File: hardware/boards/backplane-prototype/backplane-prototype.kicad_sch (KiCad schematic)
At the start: 17 parts, among them J1 DC_IN, J10 SLOT_3_IO, J11 SLOT_4_IO, J12 SLOT_5_IO, J13 SLOT_6_IO, J2 SLOT_1, J3 SLOT_2, J4 SLOT_3, J5 SLOT_4, J6 SLOT_5, J7 SLOT_6, J8 SLOT_1_IO, J9 SLOT_2_IO

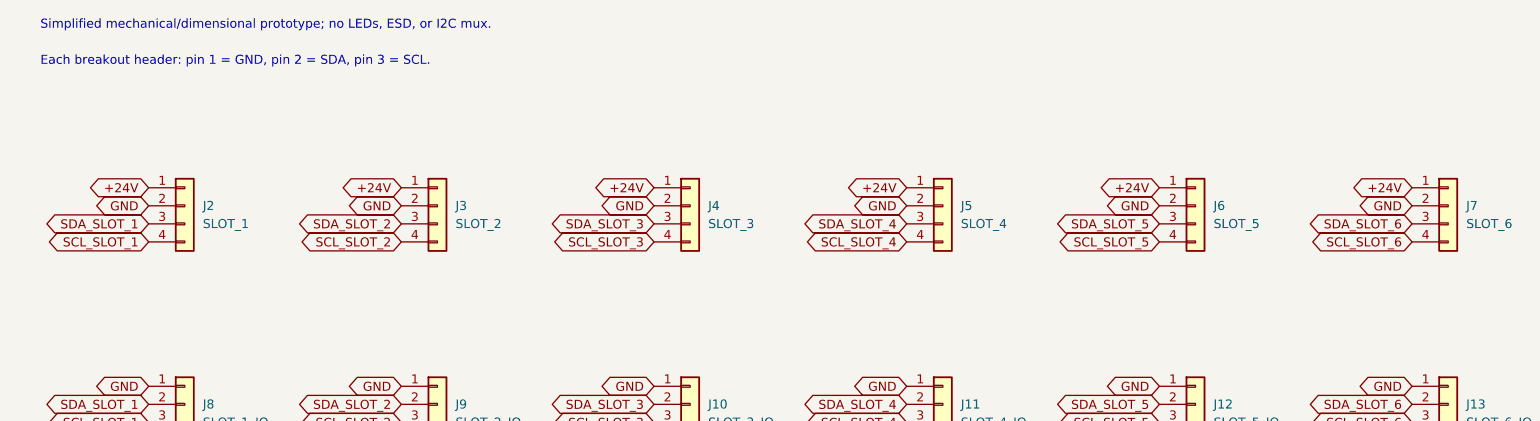
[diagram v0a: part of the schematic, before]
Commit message: Mirror prototype slot pinout changes
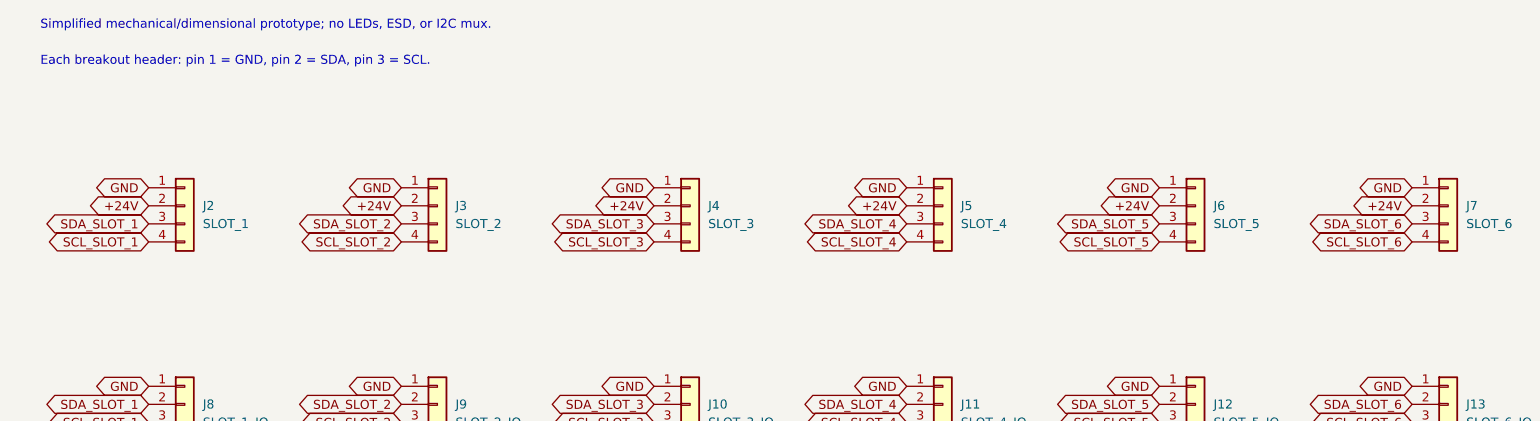
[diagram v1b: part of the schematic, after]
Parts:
- J2, J3, J4, J5, J6, J7: Pinout 1=+24V; 2=GND; 3=SDA; 4=SCL -> 1=GND; 2=+24V; 3=SDA; 4=SCL
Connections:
- net +24V: now also J2.2 (Pin_2), J3.2 (Pin_2), J4.2 (Pin_2), J5.2 (Pin_2), J6.2 (Pin_2), J7.2 (Pin_2); no longer J2.1 (Pin_1), J3.1 (Pin_1), J4.1 (Pin_1), J5.1 (Pin_1), J6.1 (Pin_1), J7.1 (Pin_1)
- net GND: now also J2.1 (Pin_1), J3.1 (Pin_1), J4.1 (Pin_1), J5.1 (Pin_1), J6.1 (Pin_1), J7.1 (Pin_1); no longer J2.2 (Pin_2), J3.2 (Pin_2), J4.2 (Pin_2), J5.2 (Pin_2), J6.2 (Pin_2), J7.2 (Pin_2)

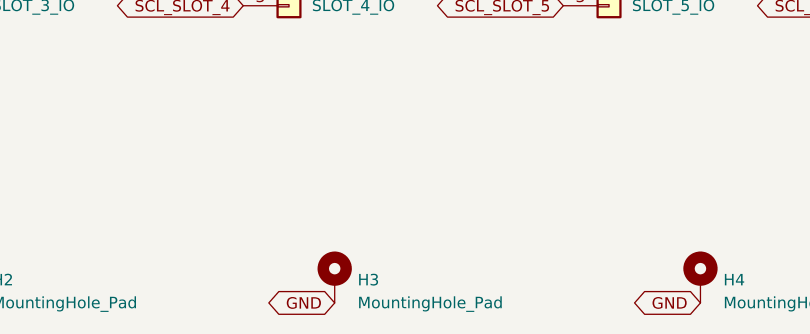
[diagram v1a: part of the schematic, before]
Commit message: Compact prototype backplane layout
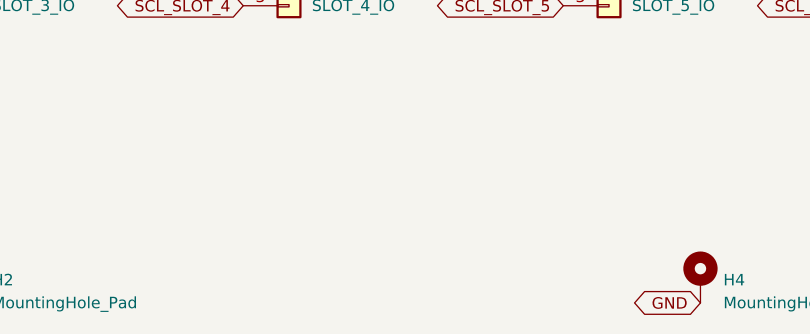
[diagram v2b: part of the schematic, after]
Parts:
- removed H3: MountingHole_Pad, MountingHole:MountingHole_3.2mm_M3_Pad_Via, symbol Mechanical:MountingHole_Pad
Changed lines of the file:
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@@
-	(global_label "GND"
-		(shape bidirectional)
-		(at 157.48 109.22 180)
-		(effects
-			(font
-				(size 1.27 1.27)
-			)
-			(justify right)
-		)
-		(property "Intersheetrefs" "${INTERSHEET_REFS}"
-			(at 157.48 109.22 0)
-			(hide yes)
-			(show_name no)
-			(do_not_autoplace no)
-			(effects
-				(font
-					(size 1.27 1.27)
-				)
-			)
-		)
-	)
 	(global_label "GND"
 		(shape bidirectional)
@@
 					(unit 1)
 				)
-			)
-		)
-	)
-	(symbol
-		(lib_id "Mechanical:MountingHole_Pad")
-		(at 157.48 106.68 0)
-		(unit 1)
-		(body_style 1)
-		(exclude_from_sim no)
-		(in_bom no)
-		(on_board yes)
-		(in_pos_files yes)
-		(dnp no)
-		(fields_autoplaced yes)
-		(property "Reference" "H3"
-			(at 160.02 106.68 0)
-			(show_name no)
-			(do_not_autoplace no)
-			(effects
-				(font
-					(size 1.27 1.27)
-				)
-				(justify left)
-			)
-		)
-		(property "Value" "MountingHole_Pad"
-			(at 160.02 109.22 0)
-			(show_name no)
-			(do_not_autoplace no)
-			(effects
-				(font
-					(size 1.27 1.27)
-				)
-				(justify left)
-			)
-		)
-		(property "Footprint" "MountingHole:MountingHole_3.2mm_M3_Pad_Via"
-			(at 157.48 106.68 0)
-			(hide yes)
-			(show_name no)
-			(do_not_autoplace no)
-			(effects
-				(font
-					(size 1.27 1.27)
-				)
-			)
-		)
-		(property "Datasheet" ""
-			(at 157.48 106.68 0)
-			(hide yes)
-			(show_name no)
-			(do_not_autoplace no)
-			(effects
-				(font
-					(size 1.27 1.27)
-				)
-			)
-		)
-		(property "Description" "Grounded M3 mounting hole"
-			(at 157.48 106.68 0)
-			(hide yes)
-			(show_name no)
-			(do_not_autoplace no)
-			(effects
-				(font
-					(size 1.27 1.27)
-				)
-			)
-		)
-		(pin "1"
-		)
-		(instances
-			(project "backplane-prototype"
-				(path "/348cc909-6345-4013-9bef-98714057a65b"
-					(reference "H3")
-					(unit 1)
-				)

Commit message: Checkpoint current hardware revisions
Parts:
- removed J10: SLOT_3_IO, Connector_PinHeader_2.54mm:PinHeader_1x03_P2.54mm_Vertical, symbol Connector_Generic:Conn_01x03
- removed J11: SLOT_4_IO, Connector_PinHeader_2.54mm:PinHeader_1x03_P2.54mm_Vertical, symbol Connector_Generic:Conn_01x03
- removed J12: SLOT_5_IO, Connector_PinHeader_2.54mm:PinHeader_1x03_P2.54mm_Vertical, symbol Connector_Generic:Conn_01x03
- removed J13: SLOT_6_IO, Connector_PinHeader_2.54mm:PinHeader_1x03_P2.54mm_Vertical, symbol Connector_Generic:Conn_01x03
- removed J8: SLOT_1_IO, Connector_PinHeader_2.54mm:PinHeader_1x03_P2.54mm_Vertical, symbol Connector_Generic:Conn_01x03
- removed J9: SLOT_2_IO, Connector_PinHeader_2.54mm:PinHeader_1x03_P2.54mm_Vertical, symbol Connector_Generic:Conn_01x03
- added H3, H5, H6: MountingHole_Pad, MountingHole:MountingHole_2.2mm_M2_Pad_Via, symbol Mechanical:MountingHole_Pad
- added J8: i2c_busses, Connector_PinHeader_1.00mm:PinHeader_2x07_P1.00mm_Vertical, symbol Connector_Generic:Conn_02x07_Odd_Even
- H1, H2, H4: footprint MountingHole:MountingHole_3.2mm_M3_Pad_Via -> MountingHole:MountingHole_2.2mm_M2_Pad_Via
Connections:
- net GND: now also H3.1, H5.1, H6.1, J8.1 (Pin_1)
- net SCL_SLOT_1: now also J8.14 (Pin_14)
- net SCL_SLOT_2: now also J8.12 (Pin_12)
- net SCL_SLOT_3: now also J8.10 (Pin_10)
- net SCL_SLOT_4: now also J8.8 (Pin_8)
- net SCL_SLOT_5: now also J8.6 (Pin_6)
- net SCL_SLOT_6: now also J8.4 (Pin_4)
- net SDA_SLOT_1: now also J8.13 (Pin_13)
- net SDA_SLOT_2: now also J8.11 (Pin_11)
- net SDA_SLOT_3: now also J8.9 (Pin_9)
- net SDA_SLOT_4: now also J8.7 (Pin_7)
- net SDA_SLOT_5: now also J8.5 (Pin_5)
- net SDA_SLOT_6: now also J8.3 (Pin_3)
- new net +3V3: J8.2 (Pin_2)
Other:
- moved on the sheet: H1, H2, H4, J1

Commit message: chore: checkpoint workspace changes
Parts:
- added D3: PESD5V0S2BT,215, Package_TO_SOT_SMD:SOT-23, symbol backplane-backpack:PESD_Dual_SOT23
- added R3, R4: 4.7k 1%, Resistor_SMD:R_0603_1608Metric, symbol Device:R
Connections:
- net +3V3: now also R3.1, R4.1
- net GND: now also D3.3 (GND)
- new net: D3.2 (IO2), R4.2
- new net: D3.1 (IO1), R3.2
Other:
- note added: "TODO: confirm pullups are / are-not already on the carrier module. If they are, DNP!"

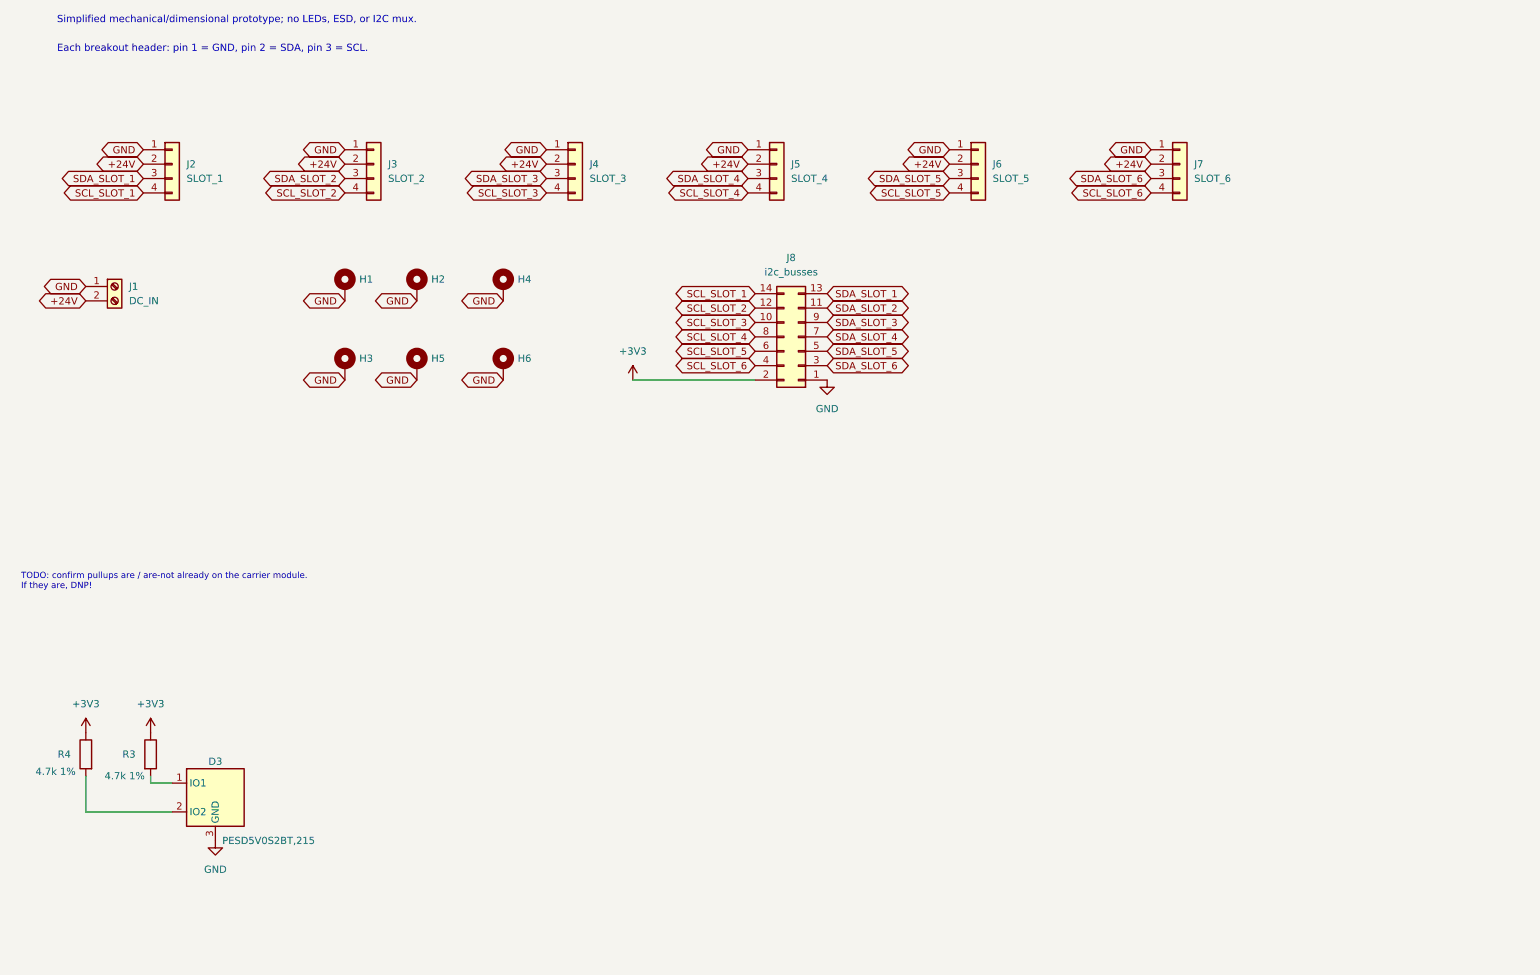
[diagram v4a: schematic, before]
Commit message: feat: add per-slot I2C ESD protection
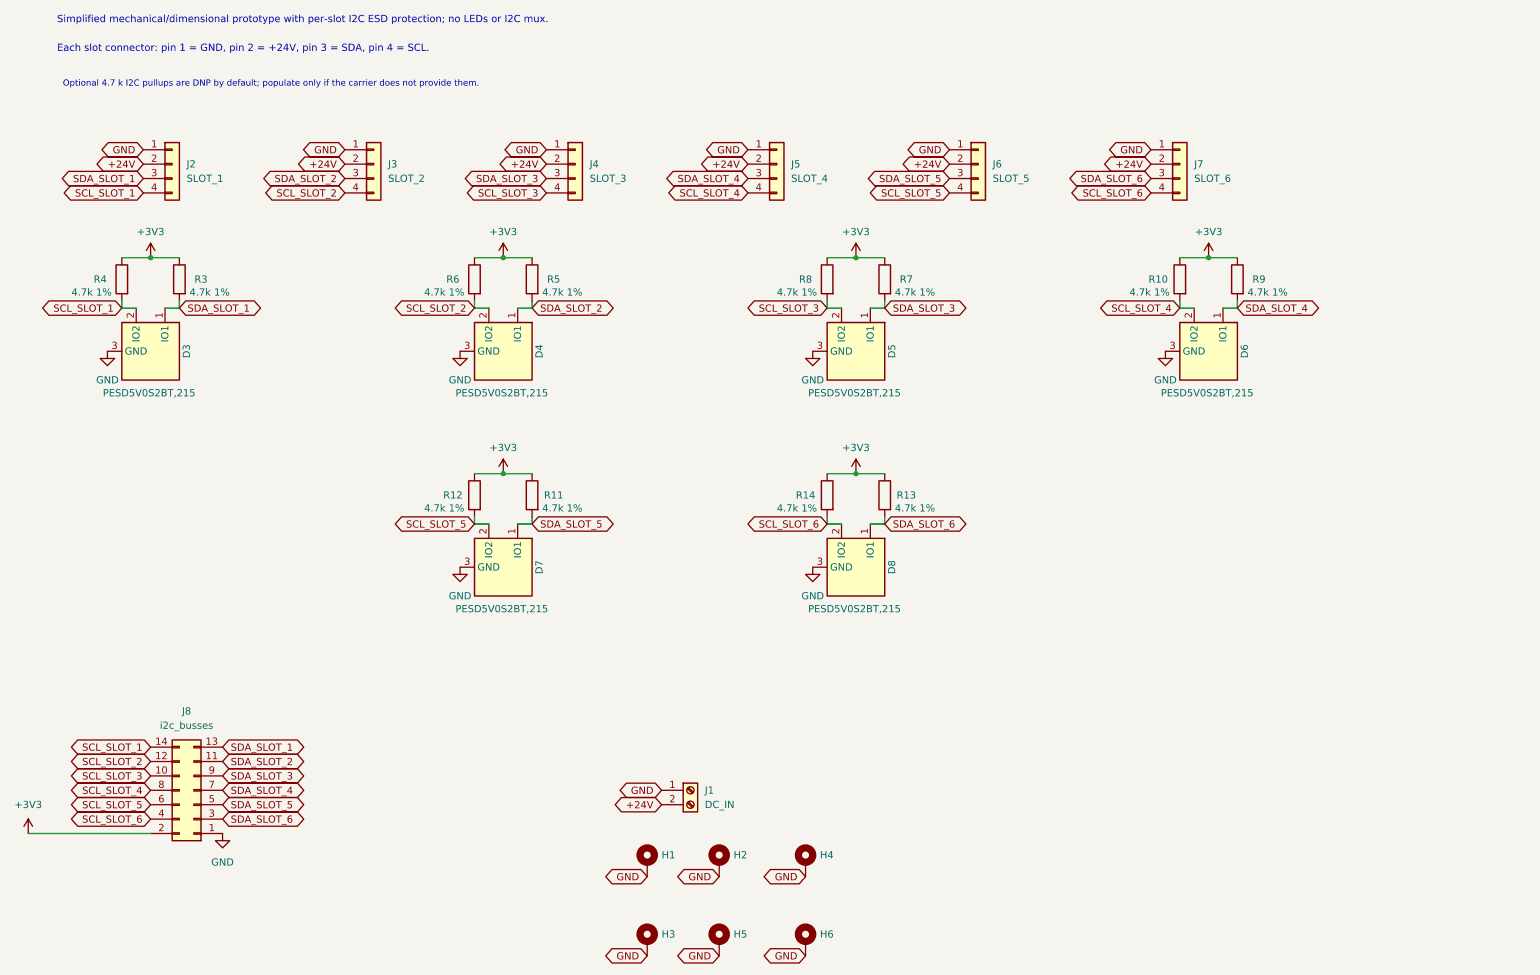
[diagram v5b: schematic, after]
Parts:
- added D4, D5, D6, D7, D8: PESD5V0S2BT,215, Package_TO_SOT_SMD:SOT-23, symbol backplane-backpack:PESD_Dual_SOT23
- added R10, R11, R12, R13, R14, R5, R6, R7, R8, R9: 4.7k 1%, Resistor_SMD:R_0603_1608Metric, symbol Device:R
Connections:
- net +3V3: now also R10.1, R11.1, R12.1, R13.1, R14.1, R5.1, R6.1, R7.1, R8.1, R9.1
- net GND: now also D4.3 (GND), D5.3 (GND), D6.3 (GND), D7.3 (GND), D8.3 (GND)
- net SCL_SLOT_1: now also D3.2 (IO2), R4.2
- net SCL_SLOT_2: now also D4.2 (IO2), R6.2
- net SCL_SLOT_3: now also D5.2 (IO2), R8.2
- net SCL_SLOT_4: now also D6.2 (IO2), R10.2
- net SCL_SLOT_5: now also D7.2 (IO2), R12.2
- net SCL_SLOT_6: now also D8.2 (IO2), R14.2
- net SDA_SLOT_1: now also D3.1 (IO1), R3.2
- net SDA_SLOT_2: now also D4.1 (IO1), R5.2
- net SDA_SLOT_3: now also D5.1 (IO1), R7.2
- net SDA_SLOT_4: now also D6.1 (IO1), R9.2
- net SDA_SLOT_5: now also D7.1 (IO1), R11.2
- net SDA_SLOT_6: now also D8.1 (IO1), R13.2
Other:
- note added: "Each slot connector: pin 1 = GND, pin 2 = +24V, pin 3 = SDA, pin 4 = SCL."
- note added: "Optional 4.7 k I2C pullups are DNP by default; populate only if the carrier does not provide them."
- note added: "Simplified mechanical/dimensional prototype with per-slot I2C ESD protection; no LEDs or I2C mux."
- note removed: "Each breakout header: pin 1 = GND, pin 2 = SDA, pin 3 = SCL."
- note removed: "Simplified mechanical/dimensional prototype; no LEDs, ESD, or I2C mux."
- note removed: "TODO: confirm pullups are / are-not already on the carrier module. If they are, DNP!"
- moved on the sheet: H1, H2, H3, H4, H5, H6, J1, J8, R3, R4

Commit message: fix: mark prototype power rails as driven
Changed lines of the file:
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@@
 	(wire
 		(pts
-			(xy 20.32 163.83) (xy 41.91 163.83)
-		)
-		(stroke
-			(width 0)
-			(type default)
-		)
-	)
-	(wire
-		(pts
 			(xy 41.91 62.23) (xy 46.99 62.23)
 		)
@@
 		)
 	)
+	(wire
+		(pts
+			(xy 54.61 163.83) (xy 60.96 163.83)
+		)
+		(stroke
+			(width 0)
+			(type default)
+		)
+	)
+	(junction
+		(at 54.61 163.83)
+		(diameter 0)
+		(color 0 0 0 0)
+	)
+	(symbol
+		(lib_id "power:PWR_FLAG")
+		(at 31.75 170.18 0)
+		(unit 1)
+		(body_style 1)
+		(exclude_from_sim no)
+		(in_bom yes)
+		(on_board yes)
+		(in_pos_files yes)
+		(dnp no)
+		(property "Reference" "#FLG0101"
+			(at 31.75 176.53 0)
+			(show_name no)
+			(do_not_autoplace no)
+			(effects
+				(font
+					(size 1.27 1.27)
+				)
+				(hide yes)
+			)
+		)
+		(property "Value" "PWR_FLAG"
+			(at 31.75 173.98999999999998 0)
+			(show_name no)
+			(do_not_autoplace no)
+			(effects
+				(font
+					(size 1.27 1.27)
+				)
+			)
+		)
+		(property "Footprint" ""
+			(at 31.75 170.18 0)
+			(hide yes)
+			(show_name no)
+			(do_not_autoplace no)
+			(effects
+				(font
+					(size 1.27 1.27)
+				)
+			)
+		)
+		(property "Datasheet" ""
+			(at 31.75 170.18 0)
+			(hide yes)
+			(show_name no)
+			(do_not_autoplace no)
+			(effects
+				(font
+					(size 1.27 1.27)
+				)
+			)
+		)
+		(property "Description" "Special symbol for telling ERC where power comes from"
+			(at 31.75 170.18 0)
+			(hide yes)
+			(show_name no)
+			(do_not_autoplace no)
+			(effects
+				(font
+					(size 1.27 1.27)
+				)
+			)
+		)
+		(pin "1"
+		)
+		(instances
+			(project "backplane-prototype"
+				(path "/348cc909-6345-4013-9bef-98714057a65b"
+					(reference "#FLG0101")
+					(unit 1)
+				)
+			)
+		)
+	)
+	(symbol
+		(lib_id "power:PWR_FLAG")
+		(at 60.96 170.18 0)
+		(unit 1)
+		(body_style 1)
+		(exclude_from_sim no)
+		(in_bom yes)
+		(on_board yes)
+		(in_pos_files yes)
+		(dnp no)
+		(property "Reference" "#FLG0102"
+			(at 60.96 176.53 0)
+			(show_name no)
+			(do_not_autoplace no)
+			(effects
+				(font
+					(size 1.27 1.27)
+				)
+				(hide yes)
+			)
+		)
+		(property "Value" "PWR_FLAG"
+			(at 60.96 173.98999999999998 0)
+			(show_name no)
+			(do_not_autoplace no)
+			(effects
+				(font
+					(size 1.27 1.27)
+				)
+			)
+		)
+		(property "Footprint" ""
+			(at 60.96 170.18 0)
+			(hide yes)
+			(show_name no)
+			(do_not_autoplace no)
+			(effects
+				(font
+					(size 1.27 1.27)
+				)
+			)
+		)
+		(property "Datasheet" ""
+			(at 60.96 170.18 0)
+			(hide yes)
+			(show_name no)
+			(do_not_autoplace no)
+			(effects
+				(font
+					(size 1.27 1.27)
+				)
+			)
+		)
+		(property "Description" "Special symbol for telling ERC where power comes from"
+			(at 60.96 170.18 0)
+			(hide yes)
+			(show_name no)
+			(do_not_autoplace no)
+			(effects
+				(font
+					(size 1.27 1.27)
+				)
+			)
+		)
+		(pin "1"
+		)
+		(instances
+			(project "backplane-prototype"
+				(path "/348cc909-6345-4013-9bef-98714057a65b"
+					(reference "#FLG0102")
+					(unit 1)
+				)
+			)
+		)
+	)
+	(wire
+		(pts
+			(xy 20.32 163.83) (xy 31.75 163.83)
+		)
+		(stroke
+			(width 0)
+			(type default)
+		)
+	)
+	(wire
+		(pts
+			(xy 31.75 163.83) (xy 41.91 163.83)
+		)
+		(stroke
+			(width 0)
+			(type default)
+		)
+	)
+	(wire
+		(pts
+			(xy 31.75 163.83) (xy 31.75 170.18)
+		)
+		(stroke
+			(width 0)
+			(type default)
+		)
+	)
+	(junction
+		(at 31.75 163.83)
+		(diameter 0)
+		(color 0 0 0 0)
+	)
+	(wire
+		(pts
+			(xy 60.96 163.83) (xy 60.96 170.18)
+		)
+		(stroke
+			(width 0)
+			(type default)
+		)
+	)

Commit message: feat: add shift-register slot power control
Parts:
- J2: Pinout 1=GND; 2=+24V; 3=SDA; 4=SCL -> 1=GND; 2=SLOT_1_PWR_SW; 3=SDA; 4=SCL
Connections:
- net +24V: no longer J2.2 (Pin_2)
- new net SLOT_1_PWR_SW: J2.2 (Pin_2)
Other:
- added sheet Slot 1 Power Switch (slot_power_switch.kicad_sch)
- note added: "Slot connectors: pin 1 = GND, pin 3 = SDA, pin 4 = SCL. J2 pin 2 is switched +24V; J3-J7 pin 2 is direct +24V."
- note removed: "Each slot connector: pin 1 = GND, pin 2 = +24V, pin 3 = SDA, pin 4 = SCL."
